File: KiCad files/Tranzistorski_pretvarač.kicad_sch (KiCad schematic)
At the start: 28 parts, among them J1 Screw_Terminal_01x02, J2 Screw_Terminal_01x02, J3 Conn_01x03_Male, J4 Conn_01x01_Male, J5 Screw_Terminal_01x03, J6 Conn_01x01_Male, J8 Conn_01x01_Male, Q1 IRLZ44N, U1 SG3524, U2 PC817

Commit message: bulk cap
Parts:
- added C?: 1000u, symbol Device:C_Polarized_Small
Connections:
- net GND: now also C?.2
- net VDD: now also C?.1
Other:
- note added: "C1-4 obavezno kvalitetni blok kondenzatori, ne elektroliti - pokušati R4 spojiti na +5V ref i vidjeti da li se išta mijenja (promijeniti i otpornik u tom slučaju) - staviti footprint za bulk cap"
- note removed: "C1-4 obavezno kvalitetni blok kondenzatori, ne elektroliti - pokušati R4 spojiti na +5V ref i vidjeti da li se išta mijenja (promijeniti i otpornik u tom slučaju)"
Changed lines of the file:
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@@
+    (stroke (width 0) (type default) (color 0 0 0 0))
+  )
+  (wire (pts (xy 121.92 43.18) (xy 121.92 45.085))
     (stroke (width 0) (type default) (color 0 0 0 0))
   )
@@
   )
   (polyline (pts (xy 194.31 110.49) (xy 194.31 35.56))
+    (stroke (width 0) (type default) (color 0 0 0 0))
+  )
+  (wire (pts (xy 111.76 43.18) (xy 121.92 43.18))
     (stroke (width 0) (type default) (color 0 0 0 0))
   )
@@
     (effects (font (size 3 3) (thickness 0.6) bold) (justify left bottom))
   )
-  (text "C1-4 obavezno kvalitetni blok kondenzatori, ne elektroliti\n\n- pokušati R4 spojiti na +5V ref i vidjeti da li se išta mijenja (promijeniti i otpornik u tom slučaju)"
+  (text "C1-4 obavezno kvalitetni blok kondenzatori, ne elektroliti\n\n- pokušati R4 spojiti na +5V ref i vidjeti da li se išta mijenja (promijeniti i otpornik u tom slučaju)\n- staviti footprint za bulk cap"
     (at 179.07 27.94 0)
     (effects (font (size 1.27 1.27)) (justify left bottom))
@@
     (pin "2")
   )
+  (symbol (lib_id "power:GND") (at 121.92 50.165 0) (unit 1)
+    (in_bom yes) (on_board yes) (fields_autoplaced)
+    (property "Reference" "#PWR?" (id 0) (at 121.92 56.515 0)
+      (effects (font (size 1.27 1.27)) hide)
+    )
+    (property "Value" "GND" (id 1) (at 121.92 54.7275 0))
+    (property "Footprint" "" (id 2) (at 121.92 50.165 0)
+      (effects (font (size 1.27 1.27)) hide)
+    )
+    (property "Datasheet" "" (id 3) (at 121.92 50.165 0)
+      (effects (font (size 1.27 1.27)) hide)
+    )
+    (pin "1")
+  )
   (symbol (lib_id "Device:C_Small") (at 54.61 99.06 0) (unit 1)
     (in_bom yes) (on_board yes) (fields_autoplaced)
@@
     )
     (property "Datasheet" "~" (id 3) (at 54.61 99.06 0)
+      (effects (font (size 1.27 1.27)) hide)
+    )
+    (pin "1")
+    (pin "2")
+  )
+  (symbol (lib_id "Device:C_Polarized_Small") (at 121.92 47.625 0) (unit 1)
+    (in_bom yes) (on_board yes) (fields_autoplaced)
+    (property "Reference" "C?" (id 0) (at 124.079 46.1704 0)
+      (effects (font (size 1.27 1.27)) (justify left))
+    )
+    (property "Value" "1000u" (id 1) (at 124.079 48.9455 0)
+      (effects (font (size 1.27 1.27)) (justify left))
+    )
+    (property "Footprint" "" (id 2) (at 121.92 47.625 0)
+      (effects (font (size 1.27 1.27)) hide)
+    )
+    (property "Datasheet" "~" (id 3) (at 121.92 47.625 0)
       (effects (font (size 1.27 1.27)) hide)
     )
@@
       (reference "#PWR0105") (unit 1) (value "VDD") (footprint "")
     )
+    (path "/bc1fdf0b-50c5-4074-9e63-2a036f703f42"
+      (reference "#PWR?") (unit 1) (value "GND") (footprint "")
+    )
     (path "/b0c859f5-da41-47d1-bec8-2ebfb3c59348"
       (reference "C1") (unit 1) (value "470n") (footprint "Capacitor_THT:C_Rect_L7.2mm_W2.5mm_P5.00mm_FKS2_FKP2_MKS2_MKP2")
@@
       (reference "C6") (unit 1) (value "100n") (footprint "Capacitor_THT:C_Rect_L7.2mm_W2.5mm_P5.00mm_FKS2_FKP2_MKS2_MKP2")
     )
+    (path "/c39275c1-7838-4ebf-8487-0dfef76f3fff"
+      (reference "C?") (unit 1) (value "1000u") (footprint "")
+    )
     (path "/4181f5e3-bbce-47d2-b8f4-8c0cc5e67930"

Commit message: update
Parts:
- C5: renamed from C?; footprint (none) -> Capacitor_THT:CP_Radial_D13.0mm_P5.00mm
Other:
- note added: "C1-4 obavezno kvalitetni blok kondenzatori, ne elektroliti - pokušati R4 spojiti na +5V ref i vidjeti da li se išta mijenja (promijeniti i otpornik u tom slučaju) - izlaz za pilu"
- note removed: "C1-4 obavezno kvalitetni blok kondenzatori, ne elektroliti - pokušati R4 spojiti na +5V ref i vidjeti da li se išta mijenja (promijeniti i otpornik u tom slučaju) - staviti footprint za bulk cap"
- moved on the sheet: H1, H2, H3, H4, J1, J2

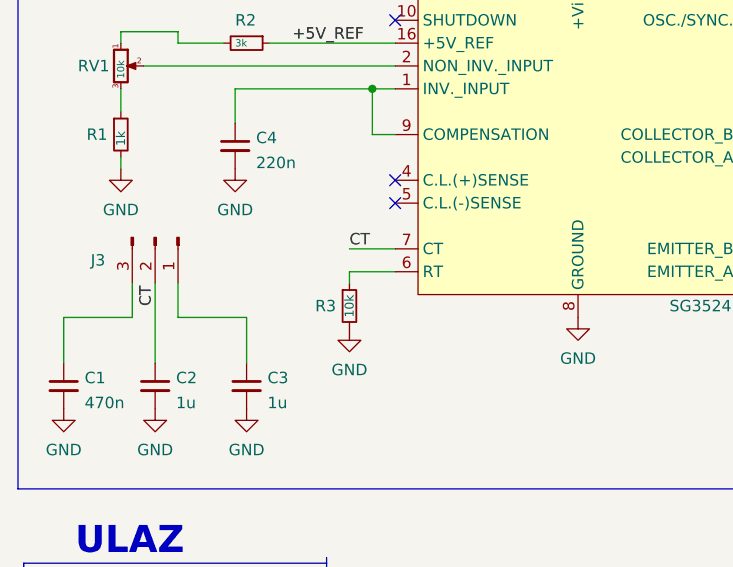
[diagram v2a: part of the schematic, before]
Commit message: added probe
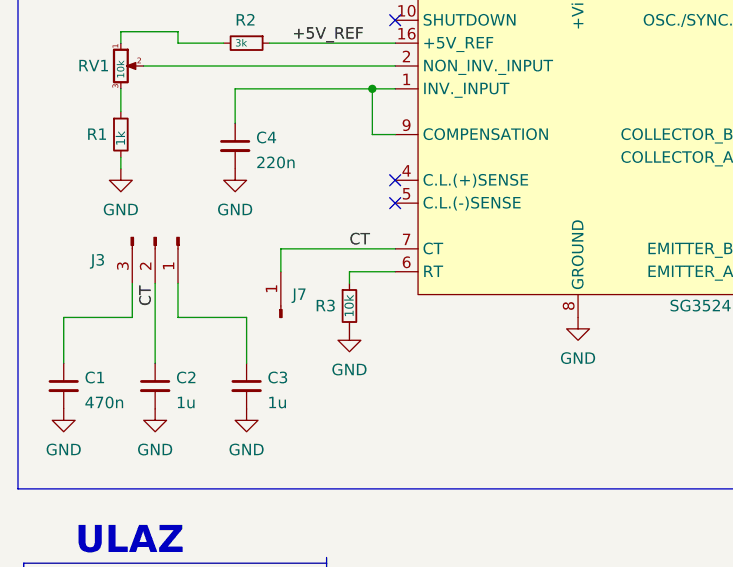
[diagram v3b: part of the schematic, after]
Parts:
- added J7: Conn_01x01_Male, footprint:oscil, symbol Connector:Conn_01x01_Male
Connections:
- net CT: now also J7.1 (Pin_1)
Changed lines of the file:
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@@
+    (stroke (width 0) (type default) (color 0 0 0 0))
+  )
+  (wire (pts (xy 68.58 83.82) (xy 81.28 83.82))
     (stroke (width 0) (type default) (color 0 0 0 0))
   )
@@
     (stroke (width 0) (type default) (color 0 0 0 0))
   )
+  (wire (pts (xy 68.58 83.82) (xy 68.58 86.36))
+    (stroke (width 0) (type default) (color 0 0 0 0))
+  )
   (polyline (pts (xy 168.91 119.38) (xy 168.91 148.59))
     (stroke (width 0) (type default) (color 0 0 0 0))
@@
   )
   (wire (pts (xy 53.34 147.32) (xy 53.34 144.78))
-    (stroke (width 0) (type default) (color 0 0 0 0))
-  )
-  (wire (pts (xy 76.2 83.82) (xy 81.28 83.82))
     (stroke (width 0) (type default) (color 0 0 0 0))
   )
@@
       (effects (font (size 1.27 1.27)) hide)
     )
+  )
+  (symbol (lib_id "Connector:Conn_01x01_Male") (at 68.58 91.44 90) (unit 1)
+    (in_bom yes) (on_board yes)
+    (property "Reference" "J7" (id 0) (at 69.85 88.9 90)
+      (effects (font (size 1.27 1.27)) (justify right))
+    )
+    (property "Value" "Conn_01x01_Male" (id 1) (at 69.4182 92.6716 90)
+      (effects (font (size 1.27 1.27)) (justify right) hide)
+    )
+    (property "Footprint" "footprint:oscil" (id 2) (at 68.58 91.44 0)
+      (effects (font (size 1.27 1.27)) hide)
+    )
+    (property "Datasheet" "~" (id 3) (at 68.58 91.44 0)
+      (effects (font (size 1.27 1.27)) hide)
+    )
+    (pin "1")
   )
   (symbol (lib_id "Connector:Conn_01x01_Male") (at 162.56 60.96 0) (unit 1)
@@
       (reference "J6") (unit 1) (value "Conn_01x01_Male") (footprint "footprint:oscil")
     )
+    (path "/13cc3ed0-5d6e-432e-a920-2485183a707f"
+      (reference "J7") (unit 1) (value "Conn_01x01_Male") (footprint "footprint:oscil")
+    )
     (path "/47de9754-16a1-48c9-846b-4a2a9dec7136"

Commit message: notes
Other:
- note added: "C1-4 obavezno kvalitetni blok kondenzatori, ne elektroliti - pokušati R4 spojiti na +5V ref i vidjeti da li se išta mijenja (promijeniti i otpornik u tom slučaju)"
- note removed: "C1-4 obavezno kvalitetni blok kondenzatori, ne elektroliti - pokušati R4 spojiti na +5V ref i vidjeti da li se išta mijenja (promijeniti i otpornik u tom slučaju) - izlaz za pilu"
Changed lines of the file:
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@@
     (effects (font (size 3 3) (thickness 0.6) bold) (justify left bottom))
   )
-  (text "C1-4 obavezno kvalitetni blok kondenzatori, ne elektroliti\n\n- pokušati R4 spojiti na +5V ref i vidjeti da li se išta mijenja (promijeniti i otpornik u tom slučaju)\n- izlaz za pilu"
+  (text "C1-4 obavezno kvalitetni blok kondenzatori, ne elektroliti\n\n- pokušati R4 spojiti na +5V ref i vidjeti da li se išta mijenja (promijeniti i otpornik u tom slučaju)"
     (at 179.07 27.94 0)
     (effects (font (size 1.27 1.27)) (justify left bottom))

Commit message: update
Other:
- note added: "C1-4 obavezno kvalitetni blok kondenzatori, ne elektroliti - staviti banana priključnice umjesto onih s vijcima"
- note removed: "C1-4 obavezno kvalitetni blok kondenzatori, ne elektroliti - pokušati R4 spojiti na +5V ref i vidjeti da li se išta mijenja (promijeniti i otpornik u tom slučaju)"
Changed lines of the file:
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@@
     (effects (font (size 3 3) (thickness 0.6) bold) (justify left bottom))
   )
-  (text "C1-4 obavezno kvalitetni blok kondenzatori, ne elektroliti\n\n- pokušati R4 spojiti na +5V ref i vidjeti da li se išta mijenja (promijeniti i otpornik u tom slučaju)"
-    (at 179.07 27.94 0)
+  (text "C1-4 obavezno kvalitetni blok kondenzatori, ne elektroliti\n\n- staviti banana priključnice umjesto onih s vijcima"
+    (at 20.32 171.45 0)
     (effects (font (size 1.27 1.27)) (justify left bottom))
   )

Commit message: shema update
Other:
- note added: "C1-4 obavezno kvalitetni blok kondenzatori, ne elektroliti - dodati banana priključnice - dodati qr kod kao link na dokumentaciju - dodati driver za mosfet ako bude potrebno (testirati pločicu barem 1h)"
- note removed: "C1-4 obavezno kvalitetni blok kondenzatori, ne elektroliti - staviti banana priključnice umjesto onih s vijcima"
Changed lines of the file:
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@@
     (effects (font (size 3 3) (thickness 0.6) bold) (justify left bottom))
   )
-  (text "C1-4 obavezno kvalitetni blok kondenzatori, ne elektroliti\n\n- staviti banana priključnice umjesto onih s vijcima"
+  (text "C1-4 obavezno kvalitetni blok kondenzatori, ne elektroliti\n\n- dodati banana priključnice\n- dodati qr kod kao link na dokumentaciju\n- dodati driver za mosfet ako bude potrebno (testirati pločicu barem 1h)"
     (at 20.32 171.45 0)
     (effects (font (size 1.27 1.27)) (justify left bottom))

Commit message: banana
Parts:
- removed J1, J2: Screw_Terminal_01x02, TerminalBlock_Phoenix:TerminalBlock_Phoenix_MKDS-1,5-2_1x02_P5.00mm_Horizontal, symbol Connector:Screw_Terminal_01x02
- added J1: Screw_Terminal_01x01, footprint:DELTRON 4mm banana socket - red, symbol Connector:Screw_Terminal_01x01
- added J2: Screw_Terminal_01x01, footprint:DELTRON 4mm banana socket - black, symbol Connector:Screw_Terminal_01x01
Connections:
- net GND: now also J2.1 (Pin_1)
- net VDD: now also J1.1 (Pin_1)
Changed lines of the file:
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@@
   (junction (at 111.76 43.18) (diameter 0) (color 0 0 0 0)
   )
-  (junction (at 53.34 129.54) (diameter 0) (color 0 0 0 0)
-  )
   (junction (at 152.4 71.12) (diameter 0) (color 0 0 0 0)
   )
@@
   )
   (junction (at 124.46 86.36) (diameter 0) (color 0 0 0 0)
-  )
-  (junction (at 53.34 144.78) (diameter 0) (color 0 0 0 0)
   )
   (junction (at 125.73 71.12) (diameter 0) (color 0 0 0 0)
@@
     (stroke (width 0) (type default) (color 0 0 0 0))
   )
-  (wire (pts (xy 53.34 142.24) (xy 53.34 144.78))
-    (stroke (width 0) (type default) (color 0 0 0 0))
-  )
   (wire (pts (xy 53.34 129.54) (xy 55.88 129.54))
     (stroke (width 0) (type default) (color 0 0 0 0))
@@
     (stroke (width 0) (type default) (color 0 0 0 0))
   )
-  (wire (pts (xy 53.34 144.78) (xy 55.88 144.78))
-    (stroke (width 0) (type default) (color 0 0 0 0))
-  )
-  (wire (pts (xy 53.34 132.08) (xy 53.34 129.54))
-    (stroke (width 0) (type default) (color 0 0 0 0))
-  )
   (wire (pts (xy 121.92 73.66) (xy 125.73 73.66))
     (stroke (width 0) (type default) (color 0 0 0 0))
   )
-  (wire (pts (xy 55.88 132.08) (xy 53.34 132.08))
-    (stroke (width 0) (type default) (color 0 0 0 0))
-  )
   (polyline (pts (xy 73.66 156.21) (xy 73.66 118.11))
     (stroke (width 0) (type default) (color 0 0 0 0))
@@
     (stroke (width 0) (type default) (color 0 0 0 0))
   )
-  (wire (pts (xy 53.34 147.32) (xy 53.34 144.78))
+  (wire (pts (xy 53.34 142.24) (xy 53.34 147.32))
     (stroke (width 0) (type default) (color 0 0 0 0))
   )
@@
     (pin "1")
     (pin "2")
+  )
+  (symbol (lib_id "Connector:Screw_Terminal_01x01") (at 60.96 129.54 0) (unit 1)
+    (in_bom yes) (on_board yes) (fields_autoplaced)
+    (property "Reference" "J1" (id 0) (at 62.992 130.019 0)
+      (effects (font (size 1.27 1.27)) (justify left))
+    )
+    (property "Value" "Screw_Terminal_01x01" (id 1) (at 62.992 131.4066 0)
+      (effects (font (size 1.27 1.27)) (justify left) hide)
+    )
+    (property "Footprint" "footprint:DELTRON 4mm banana socket - red" (id 2) (at 60.96 129.54 0)
+      (effects (font (size 1.27 1.27)) hide)
+    )
+    (property "Datasheet" "~" (id 3) (at 60.96 129.54 0)
+      (effects (font (size 1.27 1.27)) hide)
+    )
+    (pin "1")
   )
   (symbol (lib_id "Device:R_Small") (at 152.4 76.2 0) (unit 1)
@@
     (pin "2")
   )
-  (symbol (lib_id "Connector:Screw_Terminal_01x02") (at 60.96 129.54 0) (unit 1)
-    (in_bom yes) (on_board yes) (fields_autoplaced)
-    (property "Reference" "J1" (id 0) (at 62.992 131.289 0)
-      (effects (font (size 1.27 1.27)) (justify left))
-    )
-    (property "Value" "Screw_Terminal_01x02" (id 1) (at 62.992 132.6766 0)
-      (effects (font (size 1.27 1.27)) (justify left) hide)
-    )
-    (property "Footprint" "TerminalBlock_Phoenix:TerminalBlock_Phoenix_MKDS-1,5-2_1x02_P5.00mm_Horizontal" (id 2) (at 60.96 129.54 0)
-      (effects (font (size 1.27 1.27)) hide)
-    )
-    (property "Datasheet" "~" (id 3) (at 60.96 129.54 0)
-      (effects (font (size 1.27 1.27)) hide)
-    )
-    (pin "1")
-    (pin "2")
-  )
   (symbol (lib_id "Device:C_Small") (at 64.77 99.06 0) (unit 1)
     (in_bom yes) (on_board yes) (fields_autoplaced)
@@
     (pin "1")
   )
+  (symbol (lib_id "Connector:Screw_Terminal_01x01") (at 60.96 142.24 0) (unit 1)
+    (in_bom yes) (on_board yes) (fields_autoplaced)
+    (property "Reference" "J2" (id 0) (at 62.992 142.719 0)
+      (effects (font (size 1.27 1.27)) (justify left))
+    )
+    (property "Value" "Screw_Terminal_01x01" (id 1) (at 62.992 144.1066 0)
+      (effects (font (size 1.27 1.27)) (justify left) hide)
+    )
+    (property "Footprint" "footprint:DELTRON 4mm banana socket - black" (id 2) (at 60.96 142.24 0)
+      (effects (font (size 1.27 1.27)) hide)
+    )
+    (property "Datasheet" "~" (id 3) (at 60.96 142.24 0)
+      (effects (font (size 1.27 1.27)) hide)
+    )
+    (pin "1")
+  )
   (symbol (lib_id "power:VDD") (at 132.08 58.42 0) (unit 1)
     (in_bom yes) (on_board yes)
@@
     )
     (pin "1")
-  )
-  (symbol (lib_id "Connector:Screw_Terminal_01x02") (at 60.96 142.24 0) (unit 1)
-    (in_bom yes) (on_board yes) (fields_autoplaced)
-    (property "Reference" "J2" (id 0) (at 62.992 143.989 0)
-      (effects (font (size 1.27 1.27)) (justify left))
-    )
-    (property "Value" "Screw_Terminal_01x02" (id 1) (at 62.992 145.3766 0)
-      (effects (font (size 1.27 1.27)) (justify left) hide)
-    )
-    (property "Footprint" "TerminalBlock_Phoenix:TerminalBlock_Phoenix_MKDS-1,5-2_1x02_P5.00mm_Horizontal" (id 2) (at 60.96 142.24 0)
-      (effects (font (size 1.27 1.27)) hide)
-    )
-    (property "Datasheet" "~" (id 3) (at 60.96 142.24 0)
-      (effects (font (size 1.27 1.27)) hide)
-    )
-    (pin "1")
-    (pin "2")
   )
   (sheet_instances
@@
       (reference "H4") (unit 1) (value "MountingHole") (footprint "footprint:MountingHole_3.2mm_M3")
     )
-    (path "/9af3ca6a-9b5a-46a2-a5b2-0e07cabda9d7"
-      (reference "J1") (unit 1) (value "Screw_Terminal_01x02") (footprint "TerminalBlock_Phoenix:TerminalBlock_Phoenix_MKDS-1,5-2_1x02_P5.00mm_Horizontal")
-    )
-    (path "/fd67a63d-9494-4519-82a4-4392a3857e63"
-      (reference "J2") (unit 1) (value "Screw_Terminal_01x02") (footprint "TerminalBlock_Phoenix:TerminalBlock_Phoenix_MKDS-1,5-2_1x02_P5.00mm_Horizontal")
+    (path "/18294f4f-7edc-4152-bf13-29a24ca720f2"
+      (reference "J1") (unit 1) (value "Screw_Terminal_01x01") (footprint "footprint:DELTRON 4mm banana socket - red")
+    )
+    (path "/f75b54a6-f0d8-4777-9edd-9684a1de31a5"
+      (reference "J2") (unit 1) (value "Screw_Terminal_01x01") (footprint "footprint:DELTRON 4mm banana socket - black")
     )
     (path "/5a703fbc-431f-40f4-ad99-bbe431b7f329"

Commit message: v2
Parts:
- removed J5: Screw_Terminal_01x03, TerminalBlock_Phoenix:TerminalBlock_Phoenix_MKDS-1,5-3_1x03_P5.00mm_Horizontal, symbol Connector:Screw_Terminal_01x03
- added J5: Screw_Terminal_01x01, footprint:DELTRON 4mm banana socket - red, symbol Connector:Screw_Terminal_01x01
- added J9: Screw_Terminal_01x01, footprint:DELTRON 4mm banana socket - black, symbol Connector:Screw_Terminal_01x01
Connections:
- net VDD: now also J5.1 (Pin_1)
- net at D2.2 (A), J4.1 (Pin_1), Q1.2 (D): now also J9.1 (Pin_1)
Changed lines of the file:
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@@
     (stroke (width 0) (type default) (color 0 0 0 0))
   )
-  (polyline (pts (xy 39.37 35.56) (xy 39.37 110.49))
+  (polyline (pts (xy 39.37 35.56) (xy 41.91 110.49))
     (stroke (width 0) (type default) (color 0 0 0 0))
   )
@@
     (stroke (width 0) (type default) (color 0 0 0 0))
   )
-  (wire (pts (xy 184.15 58.42) (xy 186.69 58.42))
-    (stroke (width 0) (type default) (color 0 0 0 0))
-  )
-  (polyline (pts (xy 194.31 35.56) (xy 39.37 35.56))
+  (polyline (pts (xy 196.85 35.56) (xy 39.37 35.56))
     (stroke (width 0) (type default) (color 0 0 0 0))
   )
@@
     (stroke (width 0) (type default) (color 0 0 0 0))
   )
-  (polyline (pts (xy 39.37 110.49) (xy 194.31 110.49))
+  (polyline (pts (xy 41.91 110.49) (xy 196.85 110.49))
     (stroke (width 0) (type default) (color 0 0 0 0))
   )
@@
     (stroke (width 0) (type default) (color 0 0 0 0))
   )
-  (polyline (pts (xy 194.31 110.49) (xy 194.31 35.56))
+  (polyline (pts (xy 196.85 110.49) (xy 196.85 35.56))
     (stroke (width 0) (type default) (color 0 0 0 0))
   )
@@
   )
   (wire (pts (xy 57.15 59.69) (xy 57.15 60.96))
-    (stroke (width 0) (type default) (color 0 0 0 0))
-  )
-  (wire (pts (xy 184.15 60.96) (xy 184.15 58.42))
     (stroke (width 0) (type default) (color 0 0 0 0))
   )
@@
     (pin "1")
   )
-  (symbol (lib_id "Connector:Screw_Terminal_01x03") (at 191.77 55.88 0) (mirror x) (unit 1)
-    (in_bom yes) (on_board yes) (fields_autoplaced)
-    (property "Reference" "J5" (id 0) (at 191.77 50.8785 0))
-    (property "Value" "Screw_Terminal_01x03" (id 1) (at 193.802 54.0134 0)
+  (symbol (lib_id "Connector:Screw_Terminal_01x01") (at 191.77 55.88 0) (unit 1)
+    (in_bom yes) (on_board yes) (fields_autoplaced)
+    (property "Reference" "J9" (id 0) (at 193.802 56.359 0)
+      (effects (font (size 1.27 1.27)) (justify left))
+    )
+    (property "Value" "Screw_Terminal_01x01" (id 1) (at 193.802 57.7466 0)
       (effects (font (size 1.27 1.27)) (justify left) hide)
     )
-    (property "Footprint" "TerminalBlock_Phoenix:TerminalBlock_Phoenix_MKDS-1,5-3_1x03_P5.00mm_Horizontal" (id 2) (at 191.77 55.88 0)
+    (property "Footprint" "footprint:DELTRON 4mm banana socket - black" (id 2) (at 191.77 55.88 0)
       (effects (font (size 1.27 1.27)) hide)
     )
@@
     )
     (pin "1")
-    (pin "2")
-    (pin "3")
   )
   (symbol (lib_id "power:GND") (at 53.34 147.32 0) (unit 1)
@@
     (pin "1")
   )
-  (symbol (lib_id "power:GND") (at 184.15 60.96 0) (unit 1)
-    (in_bom yes) (on_board yes) (fields_autoplaced)
-    (property "Reference" "#PWR023" (id 0) (at 184.15 67.31 0)
-      (effects (font (size 1.27 1.27)) hide)
-    )
-    (property "Value" "GND" (id 1) (at 184.15 65.5225 0))
-    (property "Footprint" "" (id 2) (at 184.15 60.96 0)
-      (effects (font (size 1.27 1.27)) hide)
-    )
-    (property "Datasheet" "" (id 3) (at 184.15 60.96 0)
-      (effects (font (size 1.27 1.27)) hide)
-    )
-    (pin "1")
-  )
   (symbol (lib_id "Mechanical:MountingHole") (at 173.99 137.16 0) (unit 1)
     (in_bom yes) (on_board yes) (fields_autoplaced)
@@
     (pin "1")
     (pin "2")
+  )
+  (symbol (lib_id "Connector:Screw_Terminal_01x01") (at 191.77 53.34 0) (unit 1)
+    (in_bom yes) (on_board yes) (fields_autoplaced)
+    (property "Reference" "J5" (id 0) (at 193.802 53.819 0)
+      (effects (font (size 1.27 1.27)) (justify left))
+    )
+    (property "Value" "Screw_Terminal_01x01" (id 1) (at 193.802 55.2066 0)
+      (effects (font (size 1.27 1.27)) (justify left) hide)
+    )
+    (property "Footprint" "footprint:DELTRON 4mm banana socket - red" (id 2) (at 191.77 53.34 0)
+      (effects (font (size 1.27 1.27)) hide)
+    )
+    (property "Datasheet" "~" (id 3) (at 191.77 53.34 0)
+      (effects (font (size 1.27 1.27)) hide)
+    )
+    (pin "1")
   )
   (symbol (lib_id "Device:C_Small") (at 64.77 99.06 0) (unit 1)
@@
       (reference "#PWR021") (unit 1) (value "VDD") (footprint "")
     )
-    (path "/90e0c106-088b-4dc3-8063-79a8789d5ec0"
-      (reference "#PWR023") (unit 1) (value "GND") (footprint "")
-    )
     (path "/6716dca0-f6f3-4a3d-b122-921d8f7321a1"
       (reference "#PWR024") (unit 1) (value "GND") (footprint "")
@@
       (reference "J4") (unit 1) (value "Conn_01x01_Male") (footprint "footprint:oscil")
     )
-    (path "/5286dee4-090c-407d-91b3-d0c19e03aa7e"
-      (reference "J5") (unit 1) (value "Screw_Terminal_01x03") (footprint "TerminalBlock_Phoenix:TerminalBlock_Phoenix_MKDS-1,5-3_1x03_P5.00mm_Horizontal")
+    (path "/9e638bcf-fa6d-4b48-9460-259b57d4aead"
+      (reference "J5") (unit 1) (value "Screw_Terminal_01x01") (footprint "footprint:DELTRON 4mm banana socket - red")
     )
     (path "/2f9fe828-55af-4f84-b700-f9e19f63cca9"
@@
       (reference "J8") (unit 1) (value "Conn_01x01_Male") (footprint "footprint:oscil")
     )
+    (path "/54da39d2-4688-4755-a16a-3c76bff3cb9b"
+      (reference "J9") (unit 1) (value "Screw_Terminal_01x01") (footprint "footprint:DELTRON 4mm banana socket - black")
+    )
     (path "/40bb1208-0574-4b9c-8a7f-a1fbec81c789"
